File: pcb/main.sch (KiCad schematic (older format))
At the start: 58 parts, among them J1 Barrel_Jack, J2 NXC digit iface, J3 NXC num iface, J4 Conn_01x03, J5 ICSP, SW1 Tactile SPST, SW2 Tactile SPST, SW3 Tactile SPST, U1 4028, U2 NCP1117-5.0_SOT223, U3 PIC24FV32KA302-I_SO, U4 DS1307Z+, Y1 8 MHz, Y2 32.768 kHz

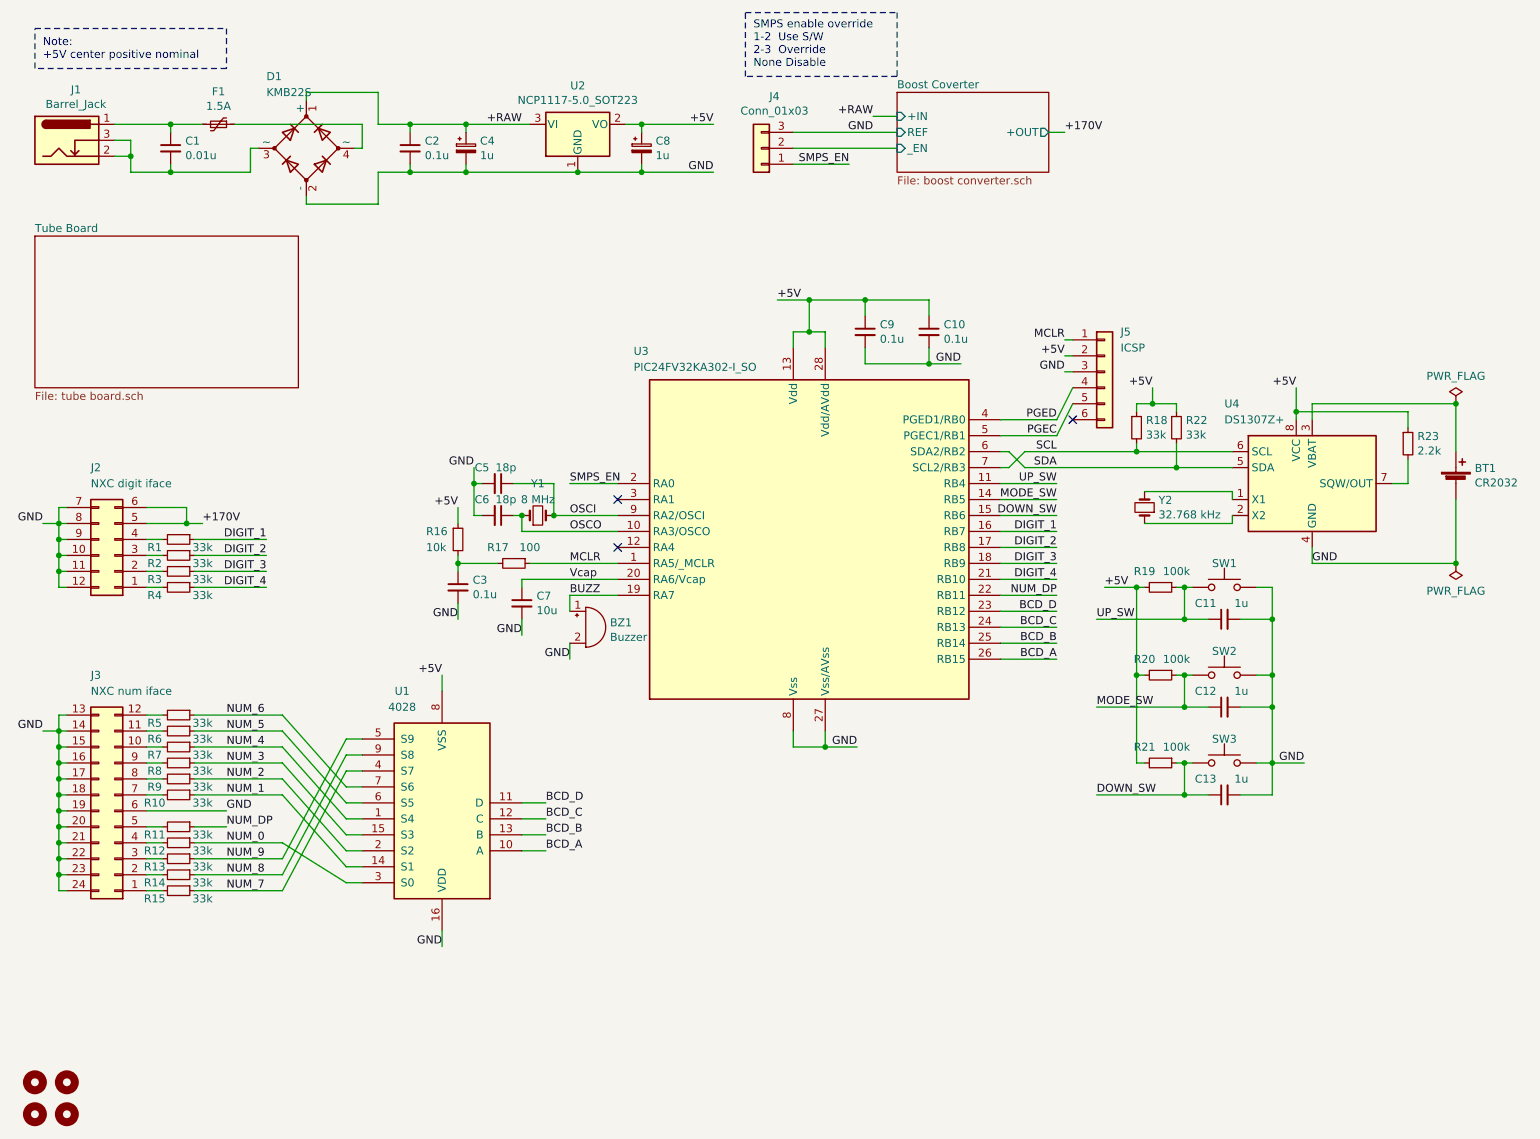
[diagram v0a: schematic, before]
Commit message: Update PCB and schematic files with mostly small tweaks. Added DRC rules added to .pro, and changes on layout and footprints to reflect that.
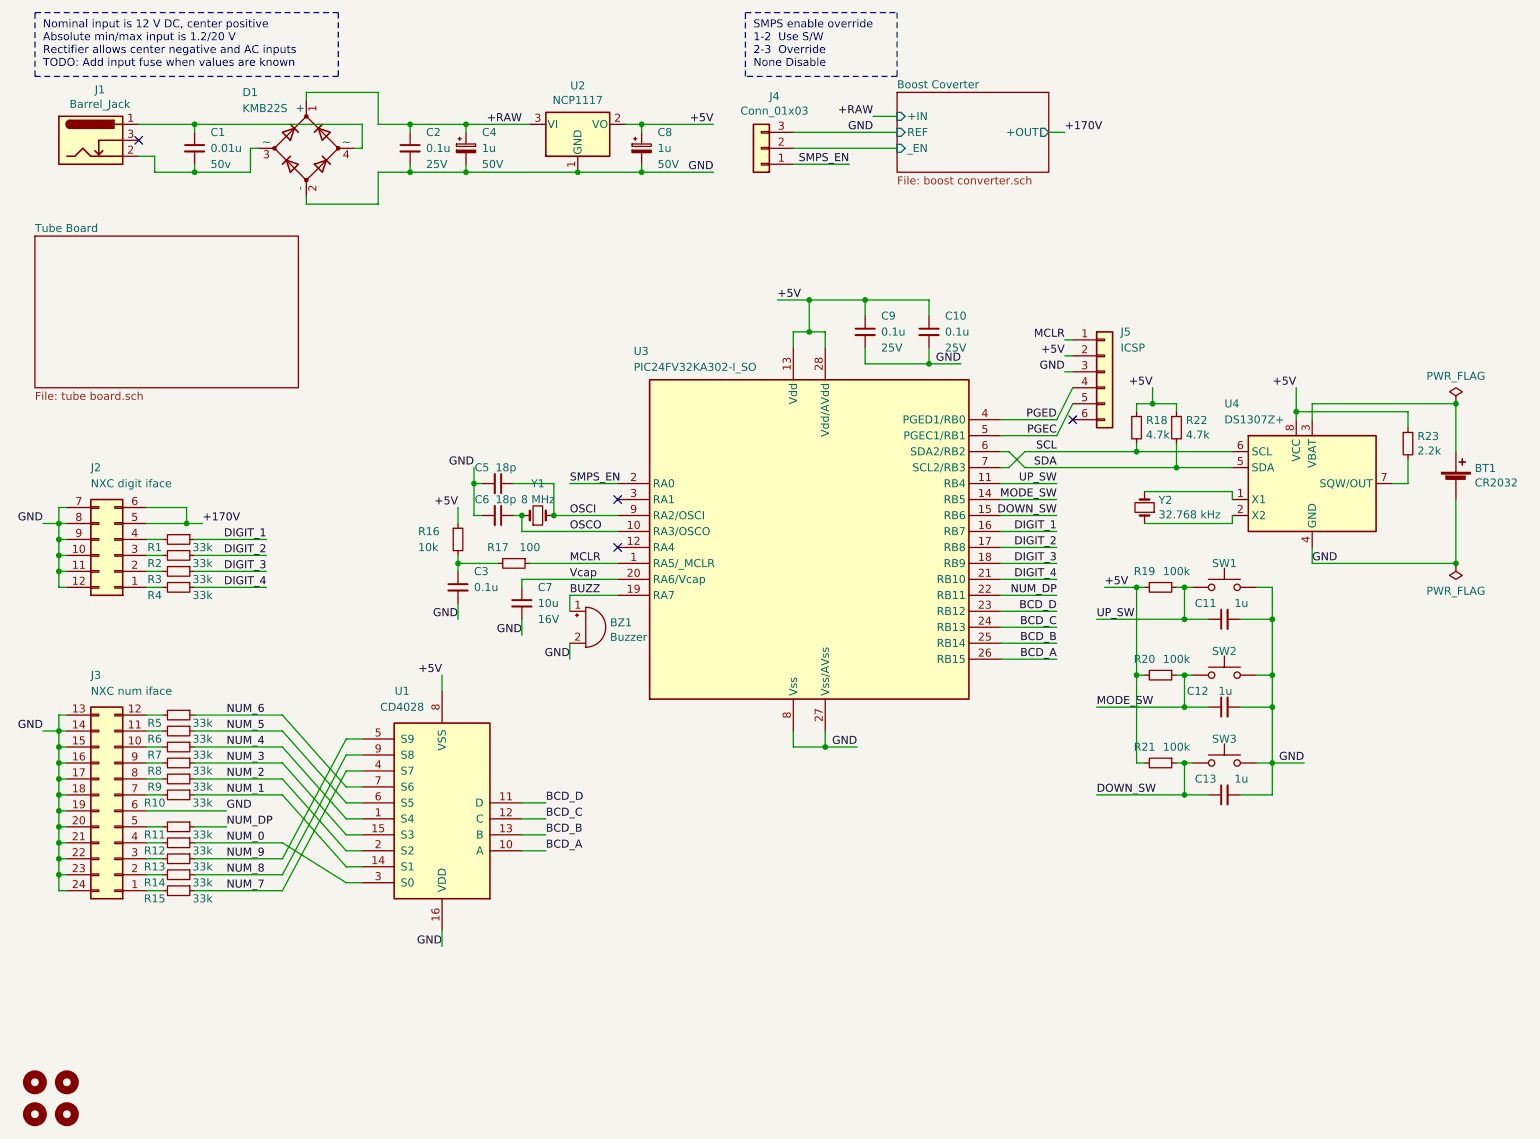
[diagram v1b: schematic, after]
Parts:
- removed F1: 1.5A, Resistors_SMD:R_0805_HandSoldering, symbol Device:Polyfuse_Small
- BT1, H1, H2, H3, H4, J1, J4, J5, SW1, SW2, SW3: Rating (none) -> N/A
- BZ1: Rating (none) -> 5V 50mA
- C1: Rating (none) -> 50v
- C10, C11, C12, C13, C2, C3, C9: Rating (none) -> 25V
- C4, C5, C6, C8: Rating (none) -> 50V
- C7: Rating (none) -> 16V
- D1: Rating (none) -> 60V
- J2, J3: Digikey Page http://www.digikey.com/product-detail/en/sullins-connector-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 -> https://www.digikey.com/en/products/detail/sullins-connecto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; Rating (none) -> N/A
- R1, R10, R11, R12, R13, R14, R15, R16, R17, R19, R2, R20, R21, R23, R3, R4, R5, R6, R7, R8, R9: Rating (none) -> 1/8W
- R18, R22: value 33k -> 4.7k; Digikey Page https://www.digikey.com/en/products/detail/yageo/RC0805FR-0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 -> https://www.digikey.com/en/products/detail/yageo/RC0805FR-1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; Rating (none) -> 1/8W
- U1: value 4028 -> CD4028; Rating (none) -> 18V
- U2: value NCP1117-5.0_SOT223 -> NCP1117; Rating (none) -> 5V
- U3: Digikey Page (none) -> https://www.digikey.com/en/products/detail/microchip-techno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; Rating (none) -> 5V
- U4: Rating (none) -> 5V
- Y1, Y2: Rating (none) -> ±20ppm
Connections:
- net at C1.1, J1.1: now also D1.4 (~~)
- net at C1.2, D1.3 (~~), J1.2: no longer J1.3
- no-connect marks 3 -> 4
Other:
- note added: "Nominal input is 12 V DC, center positive\nAbsolute min/max input is 1.2/20 V\nRectifier allows center negative and AC inputs\nTODO: Add input fuse when values are known"
- note removed: "Note:\n+5V center positive nominal"
- moved on the sheet: C1, J1

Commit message: Add alternate parts for BOM, adjust micro to be more compatible with new PIC24FJ series parts.
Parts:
- BT1: Alt Datasheet (none) -> https://www.memoryprotectiondevices.com/datasheets/BU2032SM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; Alt Digikey (none) -> https://www.digikey.com/en/products/detail/mpd-memory-prote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
- BZ1, C1, C10, C11, C12, C13, C2, C3, C5, C6, C7, C9, D1, H1, H2, H3, H4, J1, J2, J3, J4, J5, R1, R10, R11, R12, R13, R14, R15, R16, R17, R18, R19, R2, R20, R21, R22, R23, R3, R4, R5, R6, R7, R8, R9, SW1, SW2, SW3, U1, U2, Y2: Alt Datasheet (none) -> -; Alt Digikey (none) -> -
- C4, C8: Alt Datasheet (none) -> https://products.nichicon.co.jp/en/pdf/XJA043/e-uwt.pdf; Alt Digikey (none) -> https://www.digikey.com/en/products/detail/nichicon/UWT1H01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
- U3: symbol nixie-clock:PIC24FV32KA302-I_SO -> nixie-clock:PIC24FJ32GP202; Alt Datasheet (none) -> https://ww1.microchip.com/downloads/en/DeviceDoc/PIC24FJ64G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; Alt Digikey (none) -> https://www.digikey.com/en/products/detail/microchip-techno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
- U4: Alt Datasheet (none) -> https://www.diodes.com/assets/Datasheets/PT7C4339-4339C.pdf; Alt Digikey (none) -> https://www.digikey.com/en/products/detail/diodes-incorpora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
- Y1: Alt Datasheet (none) -> https://ecsxtal.com/store/pdf/ecx-53r.pdf; Alt Digikey (none) -> https://www.digikey.com/en/products/detail/ecs-inc/ECS-80-1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
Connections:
- net BUZZ: now also U3.12 (RA4); no longer U3.19 (RA7)
- net GND: now also U3.19 (Vss)
- no-connect marks 4 -> 3

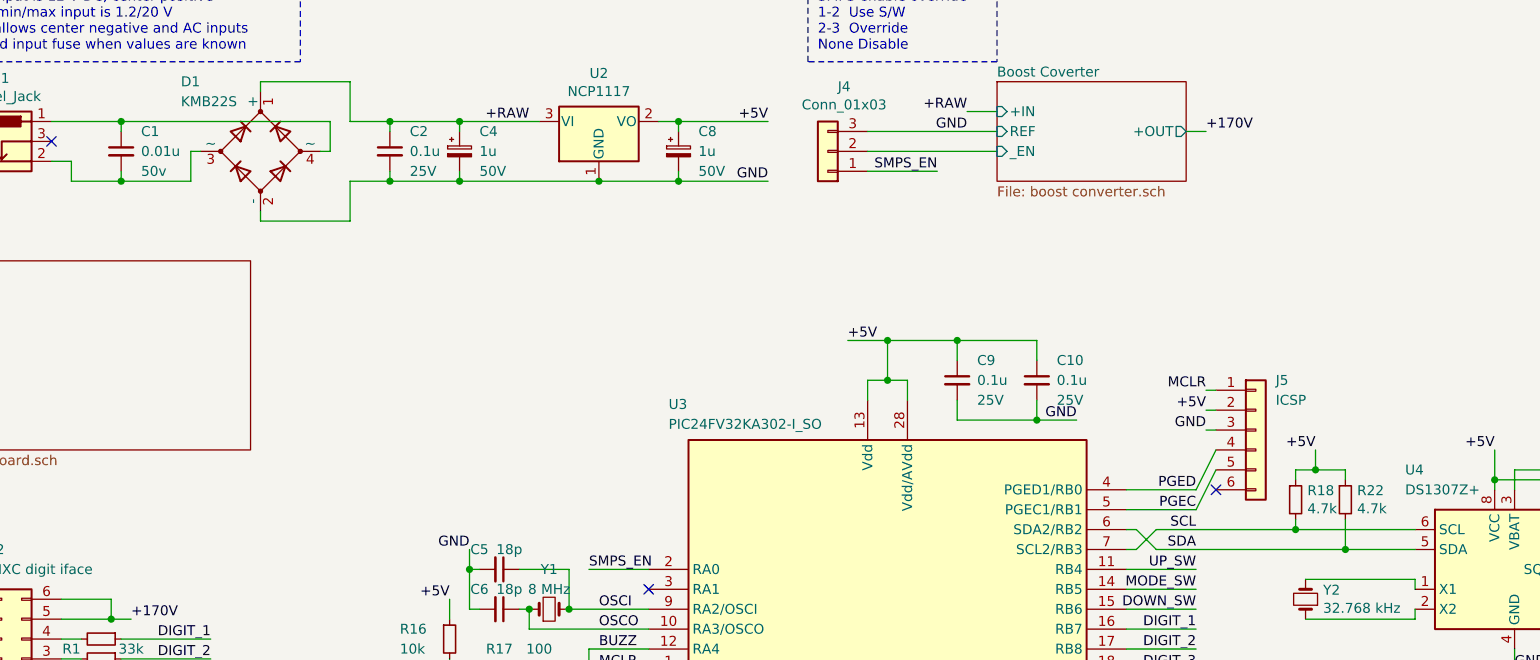
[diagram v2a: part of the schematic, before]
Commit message: Update schematic with some better part selection, reducing BOM. Update PCB for panelized fabrication.
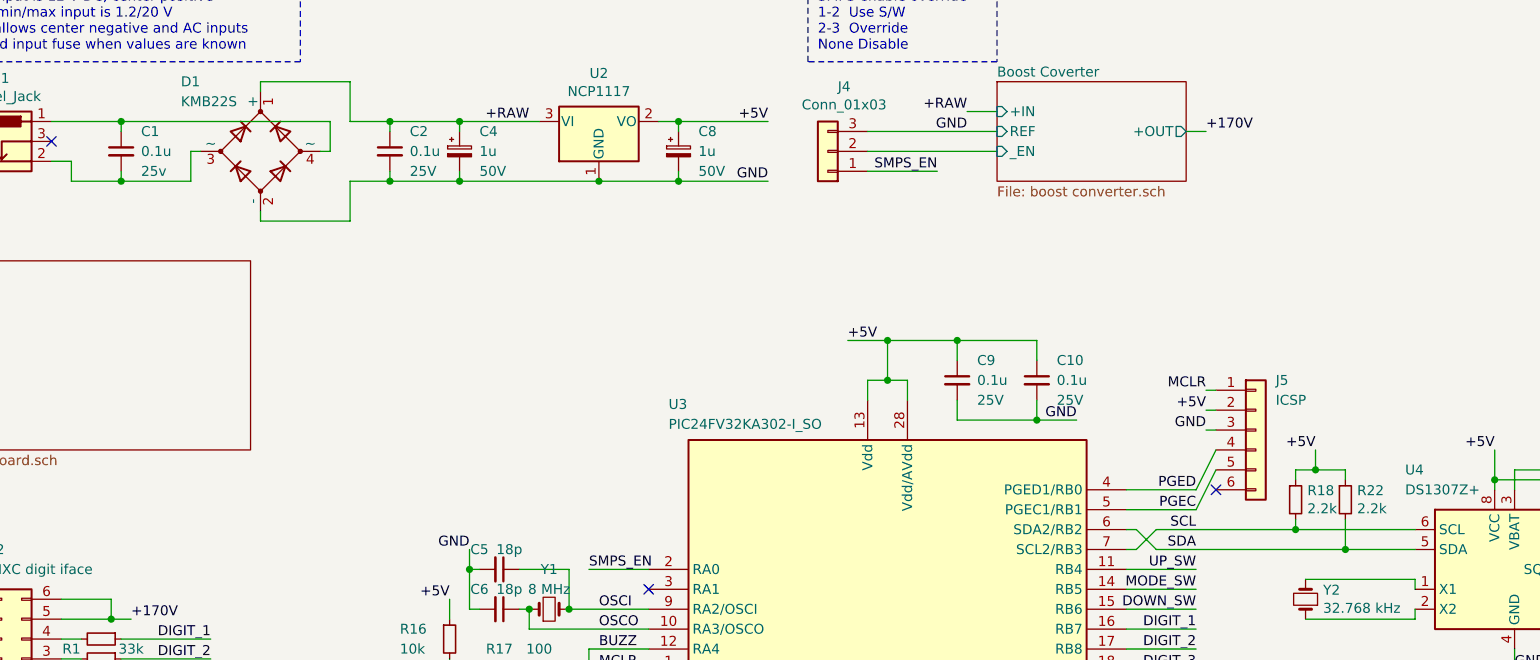
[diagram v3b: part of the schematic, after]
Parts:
- C1: value 0.01u -> 0.1u; Digikey Page https://www.digikey.com/en/products/detail/samsung-electro-mechanics/CL21B103KBANNNC/3886673 -> https://www.digikey.com/en/products/detail/samsung-electro-mechanics/CL05A104KA5NNNC/3886701; Rating 50v -> 25v
- R18, R22: value 4.7k -> 2.2k; Digikey Page https://www.digikey.com/en/products/detail/yageo/RC0805FR-1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 -> https://www.digikey.com/en/products/detail/yageo/RC0805FR-0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
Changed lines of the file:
@@
 P 1800 1450
 F 0 "C1" H 1900 1550 50  0000 L CNN
-F 1 "0.01u" H 1900 1450 50  0000 L CNN
+F 1 "0.1u" H 1900 1450 50  0000 L CNN
 F 2 "Capacitors_SMD:C_0805_HandSoldering" H 1800 1450 50  0001 C CNN
-F 3 "http://www.samsungsem.com/kr/support/product-search/mlcc/CL21B103KBANNNC.jsp" H 1800 1450 50  0001 C CNN
-F 4 "https://www.digikey.com/en/products/detail/samsung-electro-mechanics/CL21B103KBANNNC/3886673" H 1800 1450 50  0001 C CNN "Digikey Page"
-F 5 "50v" H 1900 1350 50  0000 L CNN "Rating"
+F 3 "https://media.digikey.com/pdf/Data%20Sheets/Samsung%20PDFs/CL05A104KA5NNNC.pdf" H 1800 1450 50  0001 C CNN
+F 4 "https://www.digikey.com/en/products/detail/samsung-electro-mechanics/CL05A104KA5NNNC/3886701" H 1800 1450 50  0001 C CNN "Digikey Page"
+F 5 "25v" H 1900 1350 50  0000 L CNN "Rating"
 F 6 "-" H 1800 1450 50  0001 C CNN "Alt Datasheet"
 F 7 "-" H 1800 1450 50  0001 C CNN "Alt Digikey"
@@
 P 7950 3200
 F 0 "R22" H 8009 3246 50  0000 L CNN
-F 1 "4.7k" H 8009 3155 50  0000 L CNN
+F 1 "2.2k" H 8009 3155 50  0000 L CNN
 F 2 "Resistors_SMD:R_0805_HandSoldering" H 7950 3200 50  0001 C CNN
 F 3 "https://www.yageo.com/upload/media/product/productsearch/datasheet/rchip/PYu-RC_Group_51_RoHS_L_11.pdf" H 7950 3200 50  0001 C CNN
-F 4 "https://www.digikey.com/en/products/detail/yageo/RC0805FR-134K7L/13694180" H 7950 3200 50  0001 C CNN "Digikey Page"
+F 4 "https://www.digikey.com/en/products/detail/yageo/RC0805FR-072K2L/727676" H 7950 3200 50  0001 C CNN "Digikey Page"
 F 5 "1/8W" H 7950 3200 50  0001 C CNN "Rating"
 F 6 "-" H 7950 3200 50  0001 C CNN "Alt Datasheet"
@@
 P 7700 3200
 F 0 "R18" H 7759 3246 50  0000 L CNN
-F 1 "4.7k" H 7759 3155 50  0000 L CNN
+F 1 "2.2k" H 7759 3155 50  0000 L CNN
 F 2 "Resistors_SMD:R_0805_HandSoldering" H 7700 3200 50  0001 C CNN
 F 3 "https://www.yageo.com/upload/media/product/productsearch/datasheet/rchip/PYu-RC_Group_51_RoHS_L_11.pdf" H 7700 3200 50  0001 C CNN
-F 4 "https://www.digikey.com/en/products/detail/yageo/RC0805FR-134K7L/13694180" H 7700 3200 50  0001 C CNN "Digikey Page"
+F 4 "https://www.digikey.com/en/products/detail/yageo/RC0805FR-072K2L/727676" H 7700 3200 50  0001 C CNN "Digikey Page"
 F 5 "1/8W" H 7700 3200 50  0001 C CNN "Rating"
 F 6 "-" H 7700 3200 50  0001 C CNN "Alt Datasheet"
